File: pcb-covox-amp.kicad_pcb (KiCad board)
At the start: 2 copper layers, 78 x 56 mm, 45 parts, among them J1 DB25, P1 USB, U1 LM386, X1 Amp, X2 Raw

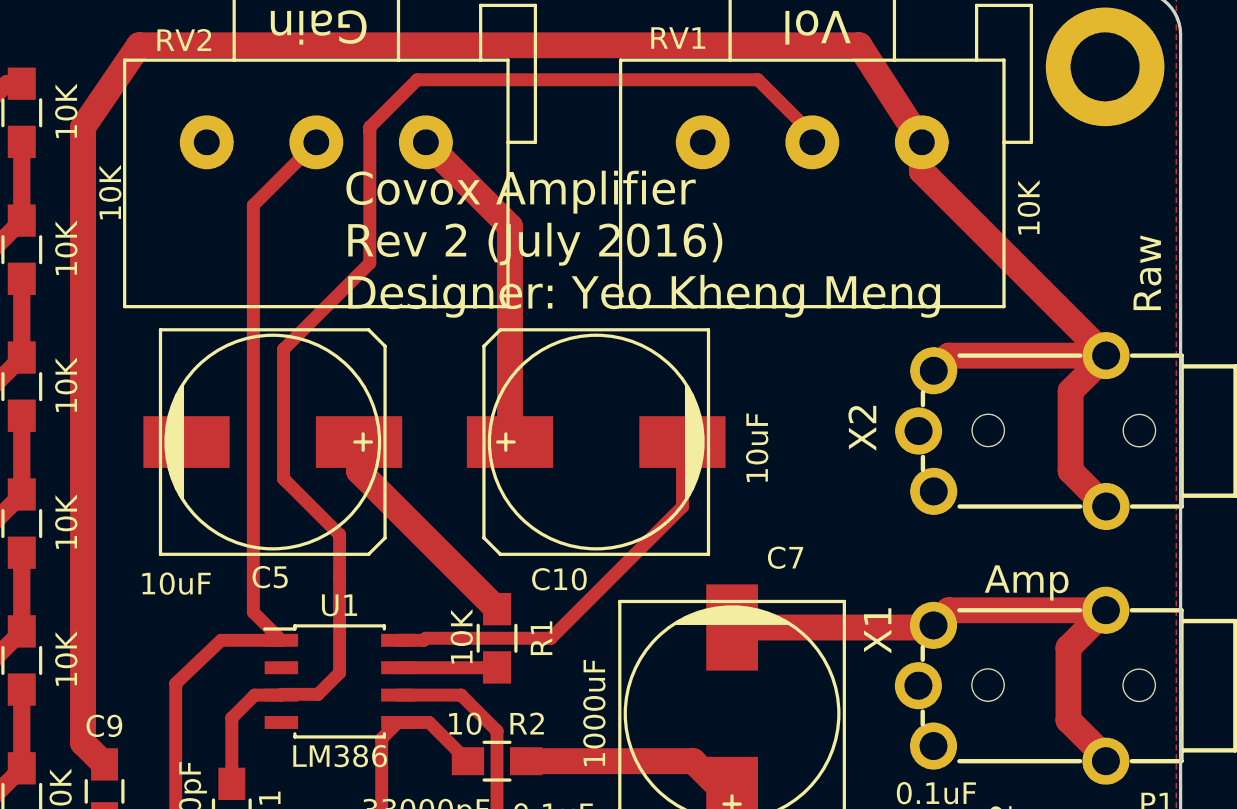
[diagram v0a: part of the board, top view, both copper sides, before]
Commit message: adjust foot print
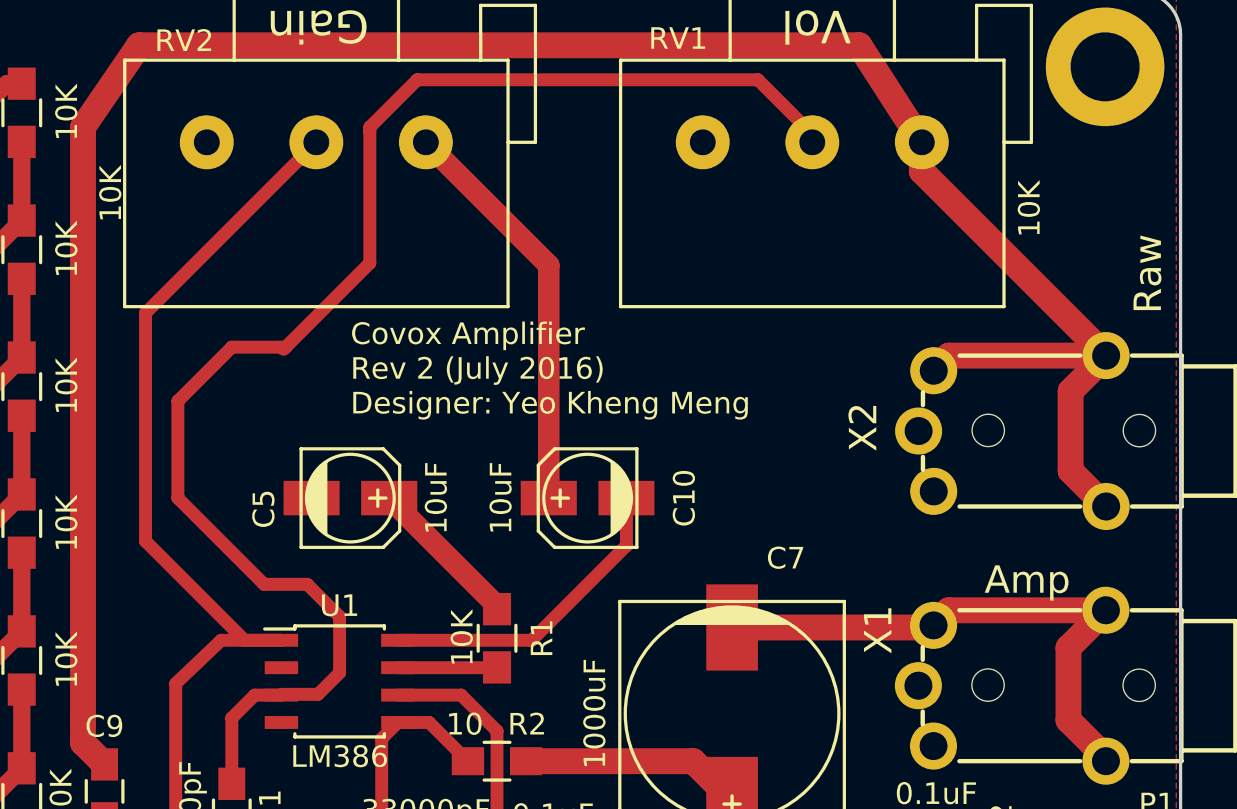
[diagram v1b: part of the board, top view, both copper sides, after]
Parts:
- C10, C5: footprint Capacitors_SMD:c_elec_10x10.5 -> Capacitors_SMD:c_elec_4x5.3
- moved C5 4.44 mm to (141.5, 109.5)
- moved C10 2.63 mm to (152.5, 109.5)
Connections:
- J1 pad 1: (no net) -> Net-(J1-Pad1)
- J1 pad 10: (no net) -> Net-(J1-Pad10)
- J1 pad 11: (no net) -> Net-(J1-Pad11)
- J1 pad 12: (no net) -> Net-(J1-Pad12)
- J1 pad 13: (no net) -> Net-(J1-Pad13)
- J1 pad 14: (no net) -> Net-(J1-Pad14)
- J1 pad 15: (no net) -> Net-(J1-Pad15)
- J1 pad 16: (no net) -> Net-(J1-Pad16)
- J1 pad 17: (no net) -> Net-(J1-Pad17)
- J1 pad 18: (no net) -> Net-(J1-Pad18)
- J1 pad 20: (no net) -> Net-(J1-Pad20)
- J1 pad 21: (no net) -> Net-(J1-Pad21)
- J1 pad 22: (no net) -> Net-(J1-Pad22)
- J1 pad 23: (no net) -> Net-(J1-Pad23)
- J1 pad 24: (no net) -> Net-(J1-Pad24)
- J1 pad 25: (no net) -> Net-(J1-Pad25)
- MH1 pad 1: (no net) -> Net-(MH1-Pad1)
- MH2 pad 1: (no net) -> Net-(MH2-Pad1)
- MH3 pad 1: (no net) -> Net-(MH3-Pad1)
- MH4 pad 1: (no net) -> Net-(MH4-Pad1)
- P1 pad 2: (no net) -> Net-(P1-Pad2)
- P1 pad 3: (no net) -> Net-(P1-Pad3)
- P1 pad 4: (no net) -> Net-(P1-Pad4)
- RV2 pad 3: (no net) -> Net-(RV2-Pad3)
- RV3 pad 3: (no net) -> Net-(RV3-Pad3)
- X1 pad P$1: (no net) -> Net-(X1-PadP$1)
- X2 pad P$1: (no net) -> Net-(X2-PadP$1)
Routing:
- net Input+: track 59.8 -> 66.6 mm
- net Gain1: track 49.6 -> 54.7 mm
- net Gain8: track 18.8 -> 14.6 mm
- net Net-(C10-Pad1): track 15.5 -> 18.9 mm
- net Net-(C5-Pad1): track 10.4 -> 7.22 mm
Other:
- net class Default: trace_width 0.8 -> 1

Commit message: adjust add pot direction
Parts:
- moved RV2 2.55 mm to (145.5, 90.5)
- moved RV1 2.50 mm to (168.0, 90.5)
- moved RV3 2.50 mm to (138.0, 137.5)
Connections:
- RV1 pad 1: Source-Audio -> GND
- RV1 pad 3: GND -> Source-Audio
- RV2 pad 1: Net-(C10-Pad1) -> Net-(RV2-Pad1)
- RV2 pad 3: Net-(RV2-Pad3) -> Net-(C10-Pad1)
- RV3 pad 1: Gain1 -> Net-(RV3-Pad1)
- RV3 pad 3: Net-(RV3-Pad3) -> Gain1
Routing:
- net Gain1: track 54.7 -> 75.4 mm
- net Source-Audio: track 103.9 -> 95.1 mm
- net Input+: track 66.6 -> 58.7 mm, vias 0 -> 1
- net Net-(C10-Pad1): track 18.9 -> 25.4 mm, vias 0 -> 1
- net Net-(C11-Pad2): track 10.4 -> 12.9 mm
- net GND: track 1.90 -> 3.38 mm

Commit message: assign all parallel pout ground pins and rev 3
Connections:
- J1 pad 1: Net-(J1-Pad1) -> (no net)
- J1 pad 10: Net-(J1-Pad10) -> (no net)
- J1 pad 11: Net-(J1-Pad11) -> (no net)
- J1 pad 12: Net-(J1-Pad12) -> (no net)
- J1 pad 13: Net-(J1-Pad13) -> (no net)
- J1 pad 14: Net-(J1-Pad14) -> (no net)
- J1 pad 15: Net-(J1-Pad15) -> (no net)
- J1 pad 16: Net-(J1-Pad16) -> (no net)
- J1 pad 17: Net-(J1-Pad17) -> (no net)
- J1 pad 18: Net-(J1-Pad18) -> GND
- J1 pad 20: Net-(J1-Pad20) -> GND
- J1 pad 21: Net-(J1-Pad21) -> GND
- J1 pad 22: Net-(J1-Pad22) -> GND
- J1 pad 23: Net-(J1-Pad23) -> GND
- J1 pad 24: Net-(J1-Pad24) -> GND
- J1 pad 25: Net-(J1-Pad25) -> GND
- MH1 pad 1: Net-(MH1-Pad1) -> (no net)
- MH2 pad 1: Net-(MH2-Pad1) -> (no net)
- MH3 pad 1: Net-(MH3-Pad1) -> (no net)
- MH4 pad 1: Net-(MH4-Pad1) -> (no net)
- P1 pad 2: Net-(P1-Pad2) -> (no net)
- P1 pad 3: Net-(P1-Pad3) -> (no net)
- P1 pad 4: Net-(P1-Pad4) -> (no net)
- RV2 pad 1: Net-(RV2-Pad1) -> (no net)
- RV3 pad 1: Net-(RV3-Pad1) -> (no net)
- X1 pad P$1: Net-(X1-PadP$1) -> (no net)
- X2 pad P$1: Net-(X2-PadP$1) -> (no net)
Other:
- board text added: "Covox Amplifier Rev 3 (July 2016) Designer: Yeo Kheng Meng"
- board text removed: "Covox Amplifier Rev 2 (July 2016) Designer: Yeo Kheng Meng"
